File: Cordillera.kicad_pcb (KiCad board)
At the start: 2 copper layers, 337.2 x 122.6 mm, 202 parts, among them Q1 AO3400, Q2 AO3400, SW1 SW_SPST, U1 STM32F072CBTx, U2 XC6206P332MR, U3 SRV05-4

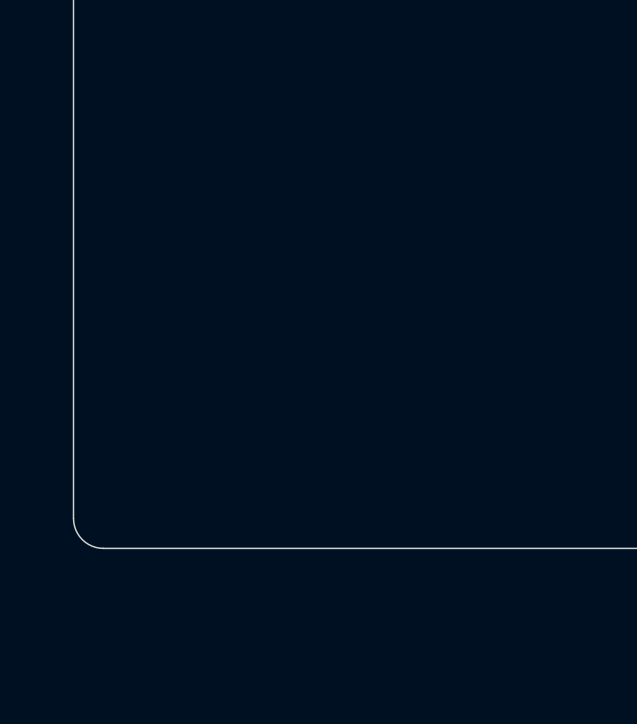
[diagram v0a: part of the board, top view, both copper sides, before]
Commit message: Add indicator LEDs
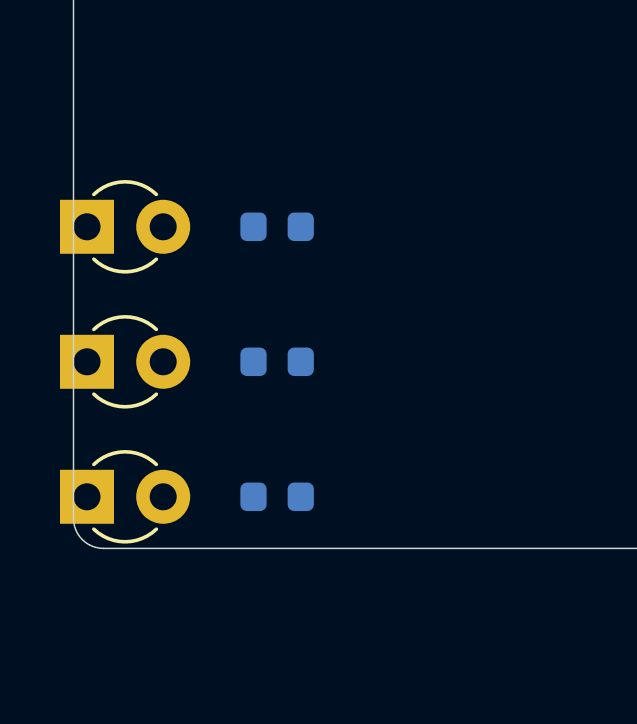
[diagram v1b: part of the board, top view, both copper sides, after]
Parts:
- added D38: LED 1, keeb_lighting:LED_D3.0mm, F.Cu at (-8.55, 76.6)
- added D39: LED 2, keeb_lighting:LED_D3.0mm, F.Cu at (-8.55, 81.1)
- added D40: LED 3, keeb_lighting:LED_D3.0mm, F.Cu at (-8.55, 85.6)
- added R75: 470, keeb_parts:R_0603_1608Metric, B.Cu at (-2.21, 76.6)
- added R76: 470, keeb_parts:R_0603_1608Metric, B.Cu at (-2.21, 81.1)
- added R77: 470, keeb_parts:R_0603_1608Metric, B.Cu at (-2.21, 85.6)

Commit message: Lay out switch and LED matrix components
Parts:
- moved D8 9.05 mm to (40.3, 55.9)
- moved D7 2.99 mm to (41.3, 36.9)
- moved D19 2.94 mm to (155.4, 14.5), turned to 258 degrees
- moved R55 2.87 mm to (229.2, 27.4), turned to 102 degrees
- moved D10 2.78 mm to (78.7, -2.60)
- moved R57 2.67 mm to (232.4, 65.7), turned to 102 degrees
- moved R51 2.50 mm to (210.5, 31.4), turned to 102 degrees
- moved R47 2.49 mm to (200.5, 53.0), turned to 102 degrees
- moved R60 2.46 mm to (248.5, 25.9), turned to 90 degrees
- moved R69 2.43 mm to (306.6, 65.1), turned to 90 degrees
- moved R53 2.30 mm to (213.8, 69.6), turned to 102 degrees
- moved R49 2.30 mm to (196.8, 92.7), turned to 102 degrees
- moved R56 2.23 mm to (237.8, 45.1), turned to 102 degrees
- moved R62 2.20 mm to (251.8, 65.1), turned to 90 degrees
- moved R42 2.17 mm to (173.3, 39.3), turned to 102 degrees
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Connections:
- R10 pad 1: Net-(KBA2-Pad4) -> /LED_GND
- R10 pad 2: /LED_GND -> Net-(KBA2-Pad4)
- R11 pad 1: Net-(KBA3-Pad4) -> /LED_GND
- R11 pad 2: /LED_GND -> Net-(KBA3-Pad4)
- R12 pad 1: Net-(KBB1-Pad4) -> /LED_GND
- R12 pad 2: /LED_GND -> Net-(KBB1-Pad4)
- R13 pad 1: Net-(KBB2-Pad4) -> /LED_GND
- R13 pad 2: /LED_GND -> Net-(KBB2-Pad4)
- R14 pad 1: Net-(KBB3-1-Pad4) -> /LED_GND
- R14 pad 2: /LED_GND -> Net-(KBB3-1-Pad4)
- R15 pad 1: Net-(KBB4-Pad4) -> /LED_GND
- R15 pad 2: /LED_GND -> Net-(KBB4-Pad4)
- R16 pad 1: Net-(KBB5-Pad4) -> /LED_GND
- R16 pad 2: /LED_GND -> Net-(KBB5-Pad4)
- R17 pad 1: Net-(KBC1-Pad4) -> /LED_GND
- R17 pad 2: /LED_GND -> Net-(KBC1-Pad4)
- R18 pad 1: Net-(KBC2-Pad4) -> /LED_GND
- R18 pad 2: /LED_GND -> Net-(KBC2-Pad4)
- R19 pad 1: Net-(KBC3-Pad4) -> /LED_GND
- R19 pad 2: /LED_GND -> Net-(KBC3-Pad4)
- R20 pad 1: Net-(KBC4-Pad4) -> /LED_GND
- R20 pad 2: /LED_GND -> Net-(KBC4-Pad4)
- R21 pad 1: Net-(KBD1-Pad4) -> /LED_GND
- R21 pad 2: /LED_GND -> Net-(KBD1-Pad4)
- R22 pad 1: Net-(KBD2-Pad4) -> /LED_GND
- R22 pad 2: /LED_GND -> Net-(KBD2-Pad4)
- R23 pad 1: Net-(KBD3-Pad4) -> /LED_GND
- R23 pad 2: /LED_GND -> Net-(KBD3-Pad4)
- R24 pad 1: Net-(KBD4-Pad4) -> /LED_GND
- R24 pad 2: /LED_GND -> Net-(KBD4-Pad4)
- R25 pad 1: Net-(KBD5-Pad4) -> /LED_GND
- R25 pad 2: /LED_GND -> Net-(KBD5-Pad4)
- R26 pad 1: Net-(KBE1-Pad4) -> /LED_GND
- R26 pad 2: /LED_GND -> Net-(KBE1-Pad4)
- R27 pad 1: Net-(KBE2-Pad4) -> /LED_GND
- R27 pad 2: /LED_GND -> Net-(KBE2-Pad4)
- R28 pad 1: Net-(KBE3-Pad4) -> /LED_GND
- R28 pad 2: /LED_GND -> Net-(KBE3-Pad4)
- R29 pad 1: Net-(KBE4-Pad4) -> /LED_GND
- R29 pad 2: /LED_GND -> Net-(KBE4-Pad4)
- R30 pad 1: Net-(KBF1-Pad4) -> /LED_GND
- R30 pad 2: /LED_GND -> Net-(KBF1-Pad4)
- R31 pad 1: Net-(KBF2-Pad4) -> /LED_GND
- R31 pad 2: /LED_GND -> Net-(KBF2-Pad4)
- R32 pad 1: Net-(KBF3-Pad4) -> /LED_GND
- R32 pad 2: /LED_GND -> Net-(KBF3-Pad4)
- R33 pad 1: Net-(KBF4-Pad4) -> /LED_GND
- R33 pad 2: /LED_GND -> Net-(KBF4-Pad4)
- R34 pad 1: Net-(KBF5-1-Pad4) -> /LED_GND
- R34 pad 2: /LED_GND -> Net-(KBF5-1-Pad4)
- R35 pad 1: Net-(KBG1-Pad4) -> /LED_GND
- R35 pad 2: /LED_GND -> Net-(KBG1-Pad4)
- R36 pad 1: Net-(KBG2-Pad4) -> /LED_GND
- R36 pad 2: /LED_GND -> Net-(KBG2-Pad4)
- R37 pad 1: Net-(KBG3-Pad4) -> /LED_GND
- R37 pad 2: /LED_GND -> Net-(KBG3-Pad4)
- R38 pad 1: Net-(KBG4-Pad4) -> /LED_GND
- R38 pad 2: /LED_GND -> Net-(KBG4-Pad4)
- R39 pad 1: Net-(KBG5-1-Pad4) -> /LED_GND
- R39 pad 2: /LED_GND -> Net-(KBG5-1-Pad4)
- R40 pad 1: Net-(KBH1-Pad4) -> /LED_GND
- R40 pad 2: /LED_GND -> Net-(KBH1-Pad4)
- R41 pad 1: Net-(KBI1-Pad4) -> /LED_GND
- R41 pad 2: /LED_GND -> Net-(KBI1-Pad4)
- R42 pad 1: Net-(KBI2-Pad4) -> /LED_GND
- R42 pad 2: /LED_GND -> Net-(KBI2-Pad4)
- R43 pad 1: Net-(KBI3-Pad4) -> /LED_GND
- R43 pad 2: /LED_GND -> Net-(KBI3-Pad4)
- R44 pad 1: Net-(KBI4-Pad4) -> /LED_GND
- R44 pad 2: /LED_GND -> Net-(KBI4-Pad4)
- R45 pad 1: Net-(KBJ1-Pad4) -> /LED_GND
- R45 pad 2: /LED_GND -> Net-(KBJ1-Pad4)
- R46 pad 1: Net-(KBJ2-Pad4) -> /LED_GND
- R46 pad 2: /LED_GND -> Net-(KBJ2-Pad4)
- R47 pad 1: Net-(KBJ3-Pad4) -> /LED_GND
- R47 pad 2: /LED_GND -> Net-(KBJ3-Pad4)
- R48 pad 1: Net-(KBJ4-Pad4) -> /LED_GND
- R48 pad 2: /LED_GND -> Net-(KBJ4-Pad4)
- R49 pad 1: Net-(KBJ5-Pad4) -> /LED_GND
- R49 pad 2: /LED_GND -> Net-(KBJ5-Pad4)
- R50 pad 1: Net-(KBK1-Pad4) -> /LED_GND
- R50 pad 2: /LED_GND -> Net-(KBK1-Pad4)
- R51 pad 1: Net-(KBK2-Pad4) -> /LED_GND
- R51 pad 2: /LED_GND -> Net-(KBK2-Pad4)
- R52 pad 1: Net-(KBK3-Pad4) -> /LED_GND
- R52 pad 2: /LED_GND -> Net-(KBK3-Pad4)
- R53 pad 1: Net-(KBK4-Pad4) -> /LED_GND
- R53 pad 2: /LED_GND -> Net-(KBK4-Pad4)
- R54 pad 1: Net-(KBL1-Pad4) -> /LED_GND
- R54 pad 2: /LED_GND -> Net-(KBL1-Pad4)
- R55 pad 1: Net-(KBL2-Pad4) -> /LED_GND
- R55 pad 2: /LED_GND -> Net-(KBL2-Pad4)
- R56 pad 1: Net-(KBL3-Pad4) -> /LED_GND
- R56 pad 2: /LED_GND -> Net-(KBL3-Pad4)
- R57 pad 1: Net-(KBL4-Pad4) -> /LED_GND
- R57 pad 2: /LED_GND -> Net-(KBL4-Pad4)
- R58 pad 1: Net-(KBL5-Pad4) -> /LED_GND
- R58 pad 2: /LED_GND -> Net-(KBL5-Pad4)
- R59 pad 1: Net-(KBM1-Pad4) -> /LED_GND
- R59 pad 2: /LED_GND -> Net-(KBM1-Pad4)
- R60 pad 1: Net-(KBM2-Pad4) -> /LED_GND
- R60 pad 2: /LED_GND -> Net-(KBM2-Pad4)
- R61 pad 1: Net-(KBM3-Pad4) -> /LED_GND
- R61 pad 2: /LED_GND -> Net-(KBM3-Pad4)
- R62 pad 1: Net-(KBM4-Pad4) -> /LED_GND
- R62 pad 2: /LED_GND -> Net-(KBM4-Pad4)
- R63 pad 1: Net-(KBN1-Pad4) -> /LED_GND
- R63 pad 2: /LED_GND -> Net-(KBN1-Pad4)
- R64 pad 1: Net-(KBN2-Pad4) -> /LED_GND
- R64 pad 2: /LED_GND -> Net-(KBN2-Pad4)
- R65 pad 1: Net-(KBN3-Pad4) -> /LED_GND
- R65 pad 2: /LED_GND -> Net-(KBN3-Pad4)
- R66 pad 1: Net-(KBN4-Pad4) -> /LED_GND
- R66 pad 2: /LED_GND -> Net-(KBN4-Pad4)
- R67 pad 1: Net-(KBO1-Pad4) -> /LED_GND
- R67 pad 2: /LED_GND -> Net-(KBO1-Pad4)
- R68 pad 1: Net-(KBO2-Pad4) -> /LED_GND
- R68 pad 2: /LED_GND -> Net-(KBO2-Pad4)
- R69 pad 1: Net-(KBO4-1-Pad4) -> /LED_GND
- R69 pad 2: /LED_GND -> Net-(KBO4-1-Pad4)
- R70 pad 1: Net-(KBP1-1-Pad4) -> /LED_GND
- R70 pad 2: /LED_GND -> Net-(KBP1-1-Pad4)
- R71 pad 1: Net-(KBP2-Pad4) -> /LED_GND
- R71 pad 2: /LED_GND -> Net-(KBP2-Pad4)
- R72 pad 1: Net-(KBP3-Pad4) -> /LED_GND
- R72 pad 2: /LED_GND -> Net-(KBP3-Pad4)
- R73 pad 1: Net-(KBP4-Pad4) -> /LED_GND
- R73 pad 2: /LED_GND -> Net-(KBP4-Pad4)
- R74 pad 1: Net-(KBP5-Pad4) -> /LED_GND
- R74 pad 2: /LED_GND -> Net-(KBP5-Pad4)
- R9 pad 1: Net-(KBA1-Pad4) -> /LED_GND
- R9 pad 2: /LED_GND -> Net-(KBA1-Pad4)

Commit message: Finish routing LED matrix
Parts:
- KBP1-1: footprint MX_Only:MXOnly-1U -> MX_Only:MXOnly-1U-FLIPPED
- moved D9 11.8 mm to (75.2, 68.3), turned to 78 degrees
- moved D35 8.89 mm to (296.8, 29.9), turned to 90 degrees
- moved D31 7.73 mm to (262.7, 29.9), turned to 90 degrees
- moved Q2 7.50 mm to (156.8, 76.9)
- moved SW1 7.50 mm to (156.4, 69.3)
- moved R8 7.50 mm to (152.5, 73.2)
- moved C11 7.50 mm to (160.7, 76.5)
- moved R7 7.50 mm to (156.8, 80.0)
- moved C12 7.50 mm to (153.5, 76.8)
- moved R4 7.45 mm to (162.6, 76.6)
- moved D18 7.43 mm to (132.4, 80.4), turned to 78 degrees
- moved D8 7.38 mm to (46.6, 52.1), turned to 90 degrees
- moved D32 7.33 mm to (259.7, 49.0), turned to 90 degrees
- moved D15 7.12 mm to (124.9, 20.4), turned to 78 degrees
- moved D13 6.99 mm to (94.5, 52.9), turned to 78 degrees
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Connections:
- KBA1 pad 2: Net-(D2-Pad1) -> Net-(D2-Pad2)
- KBA2 pad 2: Net-(D3-Pad1) -> Net-(D3-Pad2)
- KBA3 pad 2: Net-(D4-Pad1) -> Net-(D4-Pad2)
- KBB1 pad 2: Net-(D5-Pad1) -> Net-(D5-Pad2)
- KBB2 pad 2: Net-(D6-Pad1) -> Net-(D6-Pad2)
- KBB3 pad 2: Net-(D7-Pad1) -> Net-(D7-Pad2)
- KBB3-1 pad 2: Net-(D7-Pad1) -> Net-(D7-Pad2)
- KBB4 pad 2: Net-(D8-Pad1) -> Net-(D8-Pad2)
- KBB5 pad 2: Net-(D9-Pad1) -> Net-(D9-Pad2)
- KBC1 pad 1: Net-(D5-Pad2) -> /Switch + LED Matrix/colC
- KBC1 pad 2: /Switch + LED Matrix/colC -> Net-(D5-Pad1)
- KBC2 pad 1: Net-(D6-Pad2) -> /Switch + LED Matrix/colC
- KBC2 pad 2: /Switch + LED Matrix/colC -> Net-(D6-Pad1)
- KBC3 pad 1: Net-(D7-Pad2) -> /Switch + LED Matrix/colC
- KBC3 pad 2: /Switch + LED Matrix/colC -> Net-(D7-Pad1)
- KBC4 pad 1: Net-(D8-Pad2) -> /Switch + LED Matrix/colC
- KBC4 pad 2: /Switch + LED Matrix/colC -> Net-(D8-Pad1)
- KBD1 pad 2: Net-(D10-Pad1) -> Net-(D10-Pad2)
- KBD2 pad 2: Net-(D11-Pad1) -> Net-(D11-Pad2)
- KBD3 pad 2: Net-(D12-Pad1) -> Net-(D12-Pad2)
- KBD4 pad 2: Net-(D13-Pad1) -> Net-(D13-Pad2)
- KBD5 pad 2: Net-(D9-Pad2) -> Net-(D9-Pad1)
- KBE1 pad 1: Net-(D10-Pad2) -> /Switch + LED Matrix/colE
- KBE1 pad 2: /Switch + LED Matrix/colE -> Net-(D10-Pad1)
- KBE2 pad 1: Net-(D11-Pad2) -> /Switch + LED Matrix/colE
- KBE2 pad 2: /Switch + LED Matrix/colE -> Net-(D11-Pad1)
- KBE3 pad 1: Net-(D12-Pad2) -> /Switch + LED Matrix/colE
- KBE3 pad 2: /Switch + LED Matrix/colE -> Net-(D12-Pad1)
- KBE4 pad 1: Net-(D13-Pad2) -> /Switch + LED Matrix/colE
- KBE4 pad 2: /Switch + LED Matrix/colE -> Net-(D13-Pad1)
- KBF1 pad 2: Net-(D14-Pad1) -> Net-(D14-Pad2)
- KBF2 pad 2: Net-(D15-Pad1) -> Net-(D15-Pad2)
- KBF3 pad 2: Net-(D16-Pad1) -> Net-(D16-Pad2)
- KBF4 pad 2: Net-(D17-Pad1) -> Net-(D17-Pad2)
- KBF5 pad 1: /Switch + LED Matrix/colF -> Net-(D18-Pad2)
- KBF5 pad 2: Net-(D18-Pad1) -> /Switch + LED Matrix/colF
- KBF5-1 pad 1: /Switch + LED Matrix/colF -> Net-(D18-Pad2)
- KBF5-1 pad 2: Net-(D18-Pad1) -> /Switch + LED Matrix/colF
- KBG1 pad 1: Net-(D14-Pad2) -> /Switch + LED Matrix/colG
- KBG1 pad 2: /Switch + LED Matrix/colG -> Net-(D14-Pad1)
- KBG2 pad 1: Net-(D15-Pad2) -> /Switch + LED Matrix/colG
- KBG2 pad 2: /Switch + LED Matrix/colG -> Net-(D15-Pad1)
- KBG3 pad 1: Net-(D16-Pad2) -> /Switch + LED Matrix/colG
- KBG3 pad 2: /Switch + LED Matrix/colG -> Net-(D16-Pad1)
- KBG4 pad 1: Net-(D17-Pad2) -> /Switch + LED Matrix/colG
- KBG4 pad 2: /Switch + LED Matrix/colG -> Net-(D17-Pad1)
- KBG5 pad 1: Net-(D18-Pad2) -> Net-(D18-Pad1)
- KBG5-1 pad 1: Net-(D18-Pad2) -> Net-(D18-Pad1)
- KBH1 pad 2: Net-(D19-Pad1) -> Net-(D19-Pad2)
- KBI1 pad 2: Net-(D20-Pad1) -> Net-(D20-Pad2)
- KBI2 pad 2: Net-(D21-Pad1) -> Net-(D21-Pad2)
- KBI3 pad 2: Net-(D22-Pad1) -> Net-(D22-Pad2)
- KBI4 pad 2: Net-(D23-Pad1) -> Net-(D23-Pad2)
- KBJ1 pad 1: Net-(D20-Pad2) -> /Switch + LED Matrix/colJ
- KBJ1 pad 2: /Switch + LED Matrix/colJ -> Net-(D20-Pad1)
- KBJ2 pad 1: Net-(D21-Pad2) -> /Switch + LED Matrix/colJ
- KBJ2 pad 2: /Switch + LED Matrix/colJ -> Net-(D21-Pad1)
- KBJ3 pad 1: Net-(D22-Pad2) -> /Switch + LED Matrix/colJ
- KBJ3 pad 2: /Switch + LED Matrix/colJ -> Net-(D22-Pad1)
- KBJ4 pad 1: Net-(D23-Pad2) -> /Switch + LED Matrix/colJ
- KBJ4 pad 2: /Switch + LED Matrix/colJ -> Net-(D23-Pad1)
- KBJ5 pad 1: Net-(D28-Pad1) -> /Switch + LED Matrix/colJ
- KBJ5 pad 2: /Switch + LED Matrix/colJ -> Net-(D28-Pad2)
- KBK1 pad 2: Net-(D24-Pad1) -> Net-(D24-Pad2)
- KBK2 pad 2: Net-(D25-Pad1) -> Net-(D25-Pad2)
- KBK3 pad 2: Net-(D26-Pad1) -> Net-(D26-Pad2)
- KBK4 pad 2: Net-(D27-Pad1) -> Net-(D27-Pad2)
- KBL1 pad 1: Net-(D24-Pad2) -> /Switch + LED Matrix/colL
- KBL1 pad 2: /Switch + LED Matrix/colL -> Net-(D24-Pad1)
- KBL2 pad 1: Net-(D25-Pad2) -> /Switch + LED Matrix/colL
- KBL2 pad 2: /Switch + LED Matrix/colL -> Net-(D25-Pad1)
- KBL3 pad 1: Net-(D26-Pad2) -> /Switch + LED Matrix/colL
- KBL3 pad 2: /Switch + LED Matrix/colL -> Net-(D26-Pad1)
- KBL4 pad 1: Net-(D27-Pad2) -> /Switch + LED Matrix/colL
- KBL4 pad 2: /Switch + LED Matrix/colL -> Net-(D27-Pad1)
- KBL5 pad 1: Net-(D28-Pad2) -> /Switch + LED Matrix/colL
- KBL5 pad 2: /Switch + LED Matrix/colL -> Net-(D28-Pad1)
- KBM1 pad 2: Net-(D29-Pad1) -> Net-(D29-Pad2)
- KBM2 pad 2: Net-(D30-Pad1) -> Net-(D30-Pad2)
- KBM3 pad 2: Net-(D31-Pad1) -> Net-(D31-Pad2)
- KBM4 pad 2: Net-(D32-Pad1) -> Net-(D32-Pad2)
- KBN1 pad 1: Net-(D29-Pad2) -> /Switch + LED Matrix/colN
- KBN1 pad 2: /Switch + LED Matrix/colN -> Net-(D29-Pad1)
- KBN2 pad 1: Net-(D30-Pad2) -> /Switch + LED Matrix/colN
- KBN2 pad 2: /Switch + LED Matrix/colN -> Net-(D30-Pad1)
- KBN3 pad 1: Net-(D31-Pad2) -> /Switch + LED Matrix/colN
- KBN3 pad 2: /Switch + LED Matrix/colN -> Net-(D31-Pad1)
- KBN4 pad 1: Net-(D32-Pad2) -> /Switch + LED Matrix/colN
- KBN4 pad 2: /Switch + LED Matrix/colN -> Net-(D32-Pad1)
- KBO1 pad 2: Net-(D33-Pad1) -> Net-(D33-Pad2)
- KBO2 pad 2: Net-(D34-Pad1) -> Net-(D34-Pad2)
- KBO4 pad 2: Net-(D36-Pad1) -> Net-(D36-Pad2)
- KBO4-1 pad 2: Net-(D36-Pad1) -> Net-(D36-Pad2)
- KBP1 pad 1: Net-(D33-Pad2) -> /Switch + LED Matrix/colP
- KBP1 pad 2: /Switch + LED Matrix/colP -> Net-(D33-Pad1)
- KBP1-1 pad 1: Net-(D33-Pad2) -> /Switch + LED Matrix/colP
- KBP1-1 pad 2: /Switch + LED Matrix/colP -> Net-(D33-Pad1)
- KBP2 pad 1: Net-(D34-Pad2) -> /Switch + LED Matrix/colP
- KBP2 pad 2: /Switch + LED Matrix/colP -> Net-(D34-Pad1)
- KBP3 pad 1: Net-(D35-Pad2) -> /Switch + LED Matrix/colP
- KBP3 pad 2: /Switch + LED Matrix/colP -> Net-(D35-Pad1)
- KBP4 pad 1: Net-(D36-Pad2) -> /Switch + LED Matrix/colP
- KBP4 pad 2: /Switch + LED Matrix/colP -> Net-(D36-Pad1)
- KBP5 pad 1: Net-(D37-Pad2) -> /Switch + LED Matrix/colP
- KBP5 pad 2: /Switch + LED Matrix/colP -> Net-(D37-Pad1)
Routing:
- net /LED_GND: track 0.00 -> 1456.6 mm
- net +5V: track 0.00 -> 1274.5 mm
- net /Switch + LED Matrix/row2: track 0.00 -> 281.9 mm
- net /Switch + LED Matrix/row1: track 0.00 -> 281.1 mm
- net /Switch + LED Matrix/row4: track 0.00 -> 262.7 mm
- net /Switch + LED Matrix/row3: track 0.00 -> 250.8 mm
- net /Switch + LED Matrix/row5: track 0.00 -> 230.6 mm
- net /Switch + LED Matrix/colP: track 0.00 -> 110.2 mm
- net /Switch + LED Matrix/colG: track 0.00 -> 97.0 mm
- net /Switch + LED Matrix/colD: track 0.00 -> 90.5 mm
- net /Switch + LED Matrix/colB: track 0.00 -> 90.0 mm
- net /Switch + LED Matrix/colL: track 0.00 -> 88.4 mm
- net /Switch + LED Matrix/colJ: track 0.00 -> 87.7 mm
- net /Switch + LED Matrix/colF: track 0.00 -> 87.4 mm
- net /Switch + LED Matrix/colO: track 0.00 -> 73.7 mm
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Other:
- outline, holes or cut-outs redrawn
- net class Default: clearance 0.2 -> 0.1905; trace_width 0.25 -> 0.2
- net class Power added: clearance 0.1905, trace_width 0.6, via_dia 0.8, via_drill 0.4
- net class USB added: clearance 0.1905, trace_width 0.2, via_dia 0.8, via_drill 0.4
- rule pad_to_mask_clearance: 0.051 -> 0.05
- rule trace_clearance: 0.2 -> 0.1905
- rule trace_min: 0.2 -> 0.127
- rule via_min_drill: 0.3 -> 0.2
- rule via_min_size: 0.4 -> 0.45

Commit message: Do some routing
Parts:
- moved D36 69.8 mm to (242.0, 65.9), turned to 270 degrees
- moved D26 56.0 mm to (172.5, 59.8), turned to 282 degrees
- moved D27 56.0 mm to (167.1, 80.4), turned to 282 degrees
- moved D4 55.4 mm to (64.8, 46.8), turned to 270 degrees
- moved D24 55.1 mm to (169.2, 21.5), turned to 282 degrees
- moved D35 52.2 mm to (247.4, 46.8), turned to 270 degrees
- moved D33 51.9 mm to (244.1, 6.58), turned to 270 degrees
- moved D3 50.8 mm to (64.0, 27.8), turned to 270 degrees
- moved D2 41.3 mm to (59.0, 6.58), turned to 270 degrees
- moved D34 40.4 mm to (257.4, 27.8), turned to 270 degrees
- moved D25 38.3 mm to (182.5, 38.1), turned to 282 degrees
- moved D7 30.5 mm to (68.5, 46.8), turned to 270 degrees
- moved D6 28.4 mm to (67.8, 27.8), turned to 270 degrees
- moved D8 28.2 mm to (71.2, 65.9), turned to 270 degrees
- moved D32 27.3 mm to (238.3, 65.9), turned to 270 degrees
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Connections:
- KBB1 pad 2: Net-(D5-Pad2) -> Net-(D5-Pad1)
- KBB2 pad 2: Net-(D6-Pad2) -> Net-(D6-Pad1)
- KBB3 pad 2: Net-(D7-Pad2) -> Net-(D7-Pad1)
- KBB3-1 pad 2: Net-(D7-Pad2) -> Net-(D7-Pad1)
- KBB4 pad 2: Net-(D8-Pad2) -> Net-(D8-Pad1)
- KBC1 pad 2: Net-(D5-Pad1) -> Net-(D5-Pad2)
- KBC2 pad 2: Net-(D6-Pad1) -> Net-(D6-Pad2)
- KBC3 pad 2: Net-(D7-Pad1) -> Net-(D7-Pad2)
- KBC4 pad 2: Net-(D8-Pad1) -> Net-(D8-Pad2)
- KBD1 pad 2: Net-(D10-Pad2) -> Net-(D10-Pad1)
- KBD2 pad 2: Net-(D11-Pad2) -> Net-(D11-Pad1)
- KBD3 pad 2: Net-(D12-Pad2) -> Net-(D12-Pad1)
- KBD4 pad 2: Net-(D13-Pad2) -> Net-(D13-Pad1)
- KBE1 pad 2: Net-(D10-Pad1) -> Net-(D10-Pad2)
- KBE2 pad 2: Net-(D11-Pad1) -> Net-(D11-Pad2)
- KBE3 pad 2: Net-(D12-Pad1) -> Net-(D12-Pad2)
- KBE4 pad 2: Net-(D13-Pad1) -> Net-(D13-Pad2)
- KBF1 pad 2: Net-(D14-Pad2) -> Net-(D14-Pad1)
- KBF2 pad 2: Net-(D15-Pad2) -> Net-(D15-Pad1)
- KBF3 pad 2: Net-(D16-Pad2) -> Net-(D16-Pad1)
- KBF4 pad 2: Net-(D17-Pad2) -> Net-(D17-Pad1)
- KBG1 pad 2: Net-(D14-Pad1) -> Net-(D14-Pad2)
- KBG2 pad 2: Net-(D15-Pad1) -> Net-(D15-Pad2)
- KBG3 pad 2: Net-(D16-Pad1) -> Net-(D16-Pad2)
- KBG4 pad 2: Net-(D17-Pad1) -> Net-(D17-Pad2)
- KBH1 pad 2: Net-(D19-Pad2) -> Net-(D19-Pad1)
- KBI1 pad 2: Net-(D20-Pad2) -> Net-(D20-Pad1)
- KBI2 pad 2: Net-(D21-Pad2) -> Net-(D21-Pad1)
- KBI3 pad 2: Net-(D22-Pad2) -> Net-(D22-Pad1)
- KBI4 pad 2: Net-(D23-Pad2) -> Net-(D23-Pad1)
- KBJ1 pad 2: Net-(D20-Pad1) -> Net-(D20-Pad2)
- KBJ2 pad 2: Net-(D21-Pad1) -> Net-(D21-Pad2)
- KBJ3 pad 2: Net-(D22-Pad1) -> Net-(D22-Pad2)
- KBJ4 pad 2: Net-(D23-Pad1) -> Net-(D23-Pad2)
- KBK1 pad 2: Net-(D24-Pad2) -> Net-(D24-Pad1)
- KBK2 pad 2: Net-(D25-Pad2) -> Net-(D25-Pad1)
- KBK3 pad 2: Net-(D26-Pad2) -> Net-(D26-Pad1)
- KBK4 pad 2: Net-(D27-Pad2) -> Net-(D27-Pad1)
- KBL1 pad 2: Net-(D24-Pad1) -> Net-(D24-Pad2)
- KBL2 pad 2: Net-(D25-Pad1) -> Net-(D25-Pad2)
- KBL3 pad 2: Net-(D26-Pad1) -> Net-(D26-Pad2)
- KBL4 pad 2: Net-(D27-Pad1) -> Net-(D27-Pad2)
- KBM1 pad 2: Net-(D29-Pad2) -> Net-(D29-Pad1)
- KBM2 pad 2: Net-(D30-Pad2) -> Net-(D30-Pad1)
- KBM3 pad 2: Net-(D31-Pad2) -> Net-(D31-Pad1)
- KBM4 pad 2: Net-(D32-Pad2) -> Net-(D32-Pad1)
- KBN1 pad 2: Net-(D29-Pad1) -> Net-(D29-Pad2)
- KBN2 pad 2: Net-(D30-Pad1) -> Net-(D30-Pad2)
- KBN3 pad 2: Net-(D31-Pad1) -> Net-(D31-Pad2)
- KBN4 pad 2: Net-(D32-Pad1) -> Net-(D32-Pad2)
- KBO1 pad 2: Net-(D33-Pad2) -> Net-(D33-Pad1)
- KBO2 pad 2: Net-(D34-Pad2) -> Net-(D34-Pad1)
- KBO4 pad 2: Net-(D36-Pad2) -> Net-(D36-Pad1)
- KBO4-1 pad 2: Net-(D36-Pad2) -> Net-(D36-Pad1)
- KBP1 pad 2: Net-(D33-Pad1) -> Net-(D33-Pad2)
- KBP1-1 pad 2: Net-(D33-Pad1) -> Net-(D33-Pad2)
- KBP2 pad 2: Net-(D34-Pad1) -> Net-(D34-Pad2)
- KBP4 pad 2: Net-(D36-Pad1) -> Net-(D36-Pad2)
- R67 pad 1: /LED_GND -> Net-(KBO1-Pad4)
- R67 pad 2: Net-(KBO1-Pad4) -> /LED_GND
- R70 pad 1: /LED_GND -> Net-(KBP1-1-Pad4)
- R70 pad 2: Net-(KBP1-1-Pad4) -> /LED_GND
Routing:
- net +5V: track 1274.5 -> 1564.7 mm
- net /Switch + LED Matrix/row2: track 281.9 -> 83.8 mm
- net /Switch + LED Matrix/row1: track 281.1 -> 83.8 mm
- net /Switch + LED Matrix/row4: track 262.7 -> 96.0 mm
- net /Switch + LED Matrix/colP: track 110.2 -> 260.0 mm
- net /Switch + LED Matrix/colO: track 73.7 -> 197.4 mm
- net /Switch + LED Matrix/row3: track 250.8 -> 131.2 mm
- net /Switch + LED Matrix/colN: track 67.3 -> 171.0 mm
- net /Switch + LED Matrix/colM: track 68.9 -> 169.6 mm
- net /LED_GND: track 1456.6 -> 1546.4 mm, vias 0 -> 8
- net /Switch + LED Matrix/colA: track 43.5 -> 126.7 mm
- net Net-(D36-Pad2): track 15.3 -> 94.8 mm
- net Net-(D24-Pad2): track 6.47 -> 79.6 mm
- net Net-(D27-Pad2): track 7.79 -> 79.6 mm
- net Net-(D26-Pad2): track 7.82 -> 79.6 mm
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
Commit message: Finish routing switches
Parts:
- USB1: moved to F.Cu
- moved D10 58.8 mm to (132.3, 19.8), turned to 258 degrees
- moved D12 58.1 mm to (139.2, 60.2), turned to 258 degrees
- moved D13 57.3 mm to (144.5, 80.8), turned to 258 degrees
- moved D11 41.7 mm to (121.4, 36.9), turned to 258 degrees
- moved D16 27.1 mm to (142.8, 61.0), turned to 258 degrees
- moved D17 27.1 mm to (148.2, 81.6), turned to 258 degrees
- moved D14 24.6 mm to (136.0, 20.6), turned to 258 degrees
- moved D19 17.8 mm to (139.7, 21.4), turned to 258 degrees
- moved D15 17.3 mm to (125.0, 37.7), turned to 258 degrees
- moved R6 6.54 mm to (151.3, 27.9)
- moved Q1 6.54 mm to (151.1, 25.4)
- moved R5 6.54 mm to (151.3, 29.8)
- moved R8 4.81 mm to (151.6, 67.8)
- moved C6 4.13 mm to (158.3, 40.5), turned to 180 degrees
- moved C11 2.76 mm to (159.3, 73.0)
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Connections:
- net Net-(U1-Pad34) renamed /SWDIO
- KBH1 pad 2: Net-(D19-Pad1) -> Net-(D19-Pad2)
- KBI1 pad 1: /Switch + LED Matrix/colI -> /B8
- KBI2 pad 1: /Switch + LED Matrix/colI -> /B8
- KBI3 pad 1: /Switch + LED Matrix/colI -> /B8
- KBI4 pad 1: /Switch + LED Matrix/colI -> /B8
- KBJ1 pad 1: /Switch + LED Matrix/colJ -> /B7
- KBJ2 pad 1: /Switch + LED Matrix/colJ -> /B7
- KBJ3 pad 1: /Switch + LED Matrix/colJ -> /B7
- KBJ4 pad 1: /Switch + LED Matrix/colJ -> /B7
- KBJ5 pad 1: /Switch + LED Matrix/colJ -> /B7
- KBK1 pad 1: /Switch + LED Matrix/colK -> /B6
- KBK2 pad 1: /Switch + LED Matrix/colK -> /B6
- KBK3 pad 1: /Switch + LED Matrix/colK -> /B6
- KBK4 pad 1: /Switch + LED Matrix/colK -> /B6
- KBL1 pad 1: /Switch + LED Matrix/colL -> /B5
- KBL2 pad 1: /Switch + LED Matrix/colL -> /B5
- KBL3 pad 1: /Switch + LED Matrix/colL -> /B5
- KBL4 pad 1: /Switch + LED Matrix/colL -> /B5
- KBL5 pad 1: /Switch + LED Matrix/colL -> /B5
- KBM1 pad 1: /Switch + LED Matrix/colM -> /B4
- KBM2 pad 1: /Switch + LED Matrix/colM -> /B4
- KBM3 pad 1: /Switch + LED Matrix/colM -> /B4
- KBM4 pad 1: /Switch + LED Matrix/colM -> /B4
- KBN1 pad 1: /Switch + LED Matrix/colN -> /B3
- KBN2 pad 1: /Switch + LED Matrix/colN -> /B3
- KBN3 pad 1: /Switch + LED Matrix/colN -> /B3
- KBN4 pad 1: /Switch + LED Matrix/colN -> /B3
- KBO1 pad 1: /Switch + LED Matrix/colO -> /A15
- KBO2 pad 1: /Switch + LED Matrix/colO -> /A15
- KBO4 pad 1: /Switch + LED Matrix/colO -> /A15
- KBO4-1 pad 1: /Switch + LED Matrix/colO -> /A15
- KBP1 pad 1: /Switch + LED Matrix/colP -> /SWDCLK
- KBP1-1 pad 1: /Switch + LED Matrix/colP -> /SWDCLK
- KBP2 pad 1: /Switch + LED Matrix/colP -> /SWDCLK
- KBP3 pad 1: /Switch + LED Matrix/colP -> /SWDCLK
- KBP4 pad 1: /Switch + LED Matrix/colP -> /SWDCLK
- KBP5 pad 1: /Switch + LED Matrix/colP -> /SWDCLK
- R2 pad 1: GND -> Net-(R2-Pad1)
- R2 pad 2: Net-(R2-Pad2) -> GND
- U1 pad 37: Net-(U1-Pad37) -> /SWDCLK
- U1 pad 38: Net-(U1-Pad38) -> /A15
- U1 pad 39: Net-(U1-Pad39) -> /B3
- U1 pad 40: Net-(U1-Pad40) -> /B4
- U1 pad 41: Net-(U1-Pad41) -> /B5
- U1 pad 42: Net-(U1-Pad42) -> /B6
- U1 pad 43: Net-(U1-Pad43) -> /B7
- U1 pad 45: Net-(U1-Pad45) -> /B8
- USB1 pad 4: Net-(R2-Pad2) -> Net-(R2-Pad1)
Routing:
- net /SWDCLK: track 0.00 -> 277.8 mm
- net /Switch + LED Matrix/colP: track 260.0 -> 0.00 mm
- net /A15: track 0.00 -> 227.7 mm
- net /Switch + LED Matrix/colO: track 197.4 -> 0.00 mm
- net /B3: track 0.00 -> 189.7 mm
- net /B4: track 0.00 -> 188.3 mm
- net +5V: track 1564.7 -> 1750.5 mm, vias 0 -> 1
- net /Switch + LED Matrix/colN: track 171.0 -> 0.00 mm
- net /B5: track 0.00 -> 169.9 mm
- net /Switch + LED Matrix/colM: track 169.6 -> 0.00 mm
- net /Switch + LED Matrix/colL: track 151.8 -> 0.00 mm
- net /B7: track 0.00 -> 130.9 mm
- net /B6: track 0.00 -> 130.0 mm
- net /Switch + LED Matrix/colJ: track 119.9 -> 0.00 mm
- net /Switch + LED Matrix/colK: track 113.0 -> 0.00 mm
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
